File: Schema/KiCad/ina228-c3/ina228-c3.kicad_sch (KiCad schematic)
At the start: 35 parts, among them J1 Terminal, U1 XL7015E1, U2 HT7833, U3 INA238, U4 ESP32-C3-WROOM-02

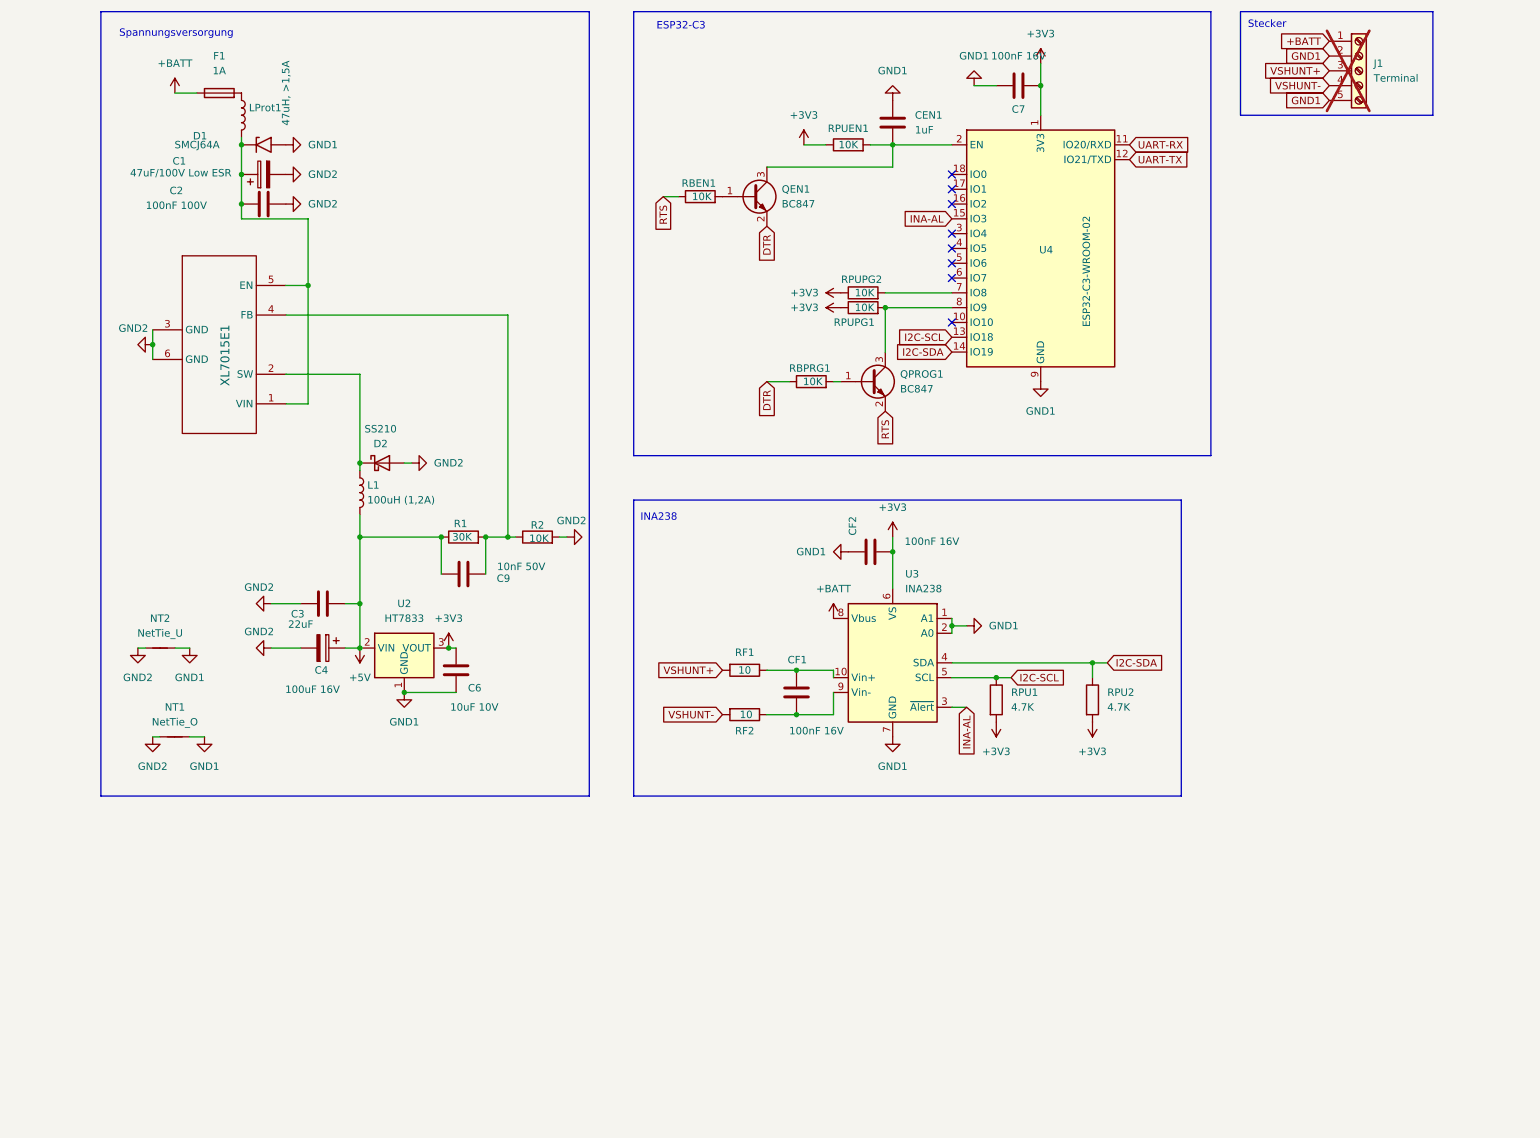
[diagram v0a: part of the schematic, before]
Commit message: Remove usb2uart chip, making the design simpler (but probably more expensive.)
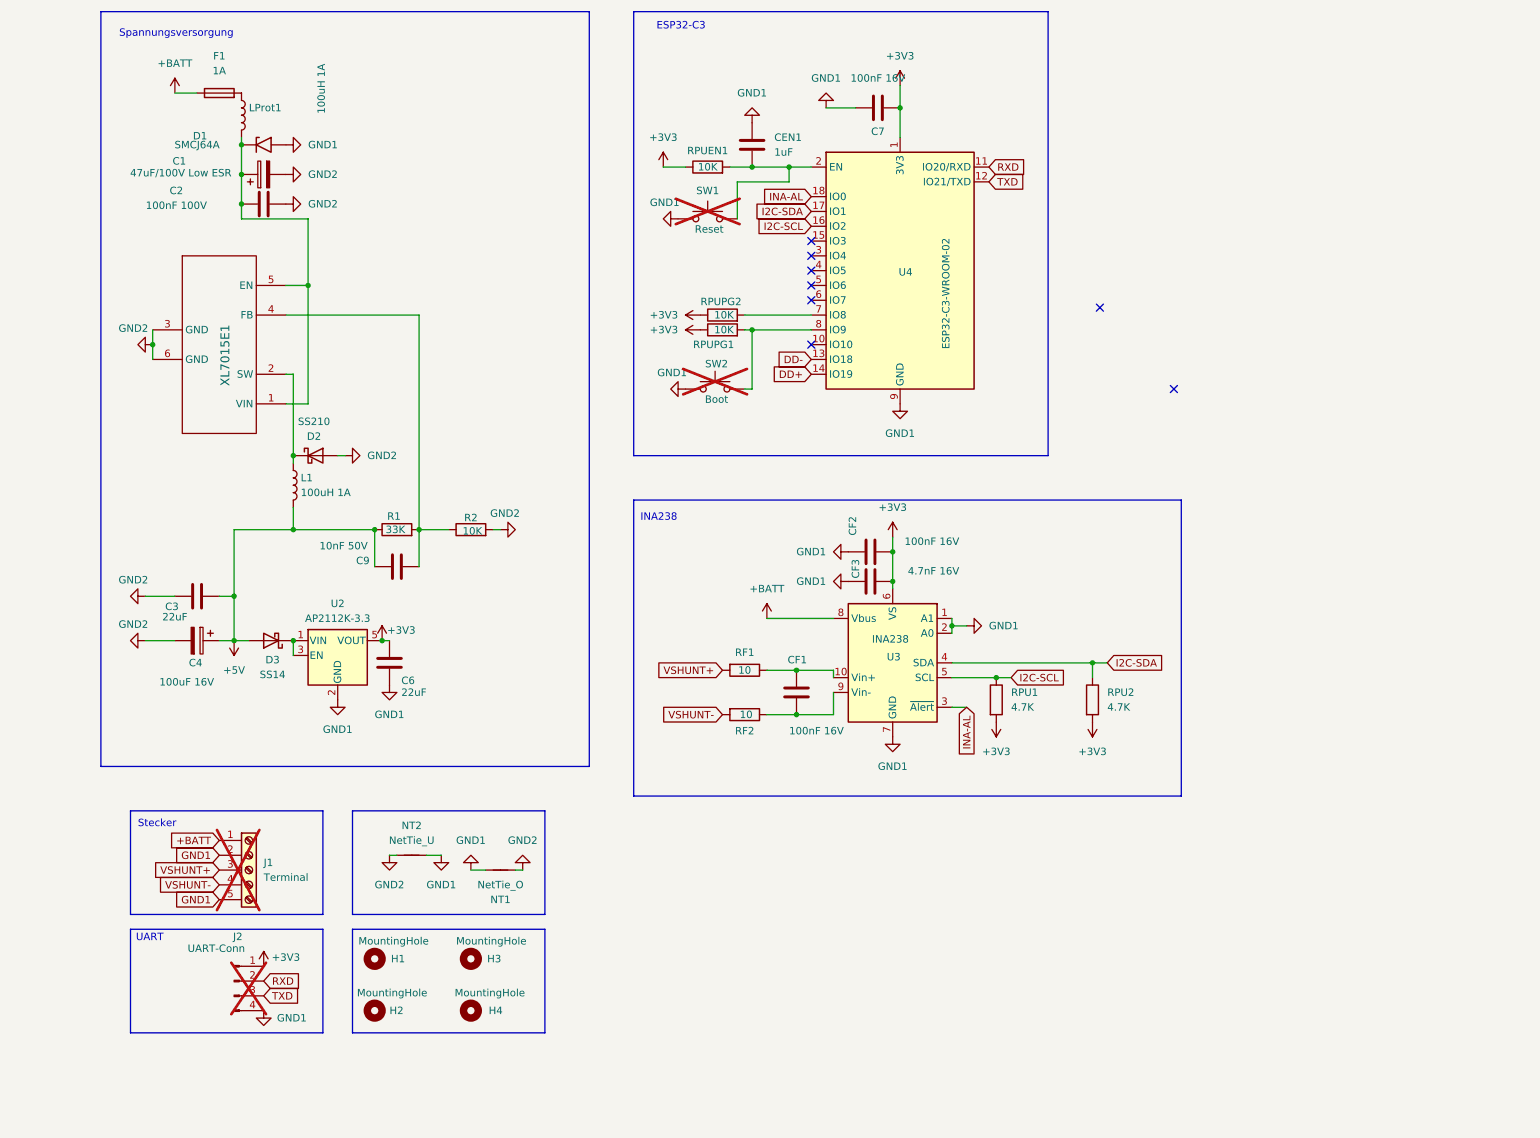
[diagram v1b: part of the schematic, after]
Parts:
- removed QEN1, QPROG1: BC847, Package_TO_SOT_SMD:SOT-23, symbol Transistor_BJT:BC847
- removed RBEN1, RBPRG1: 10K, Resistor_SMD:R_0603_1608Metric, symbol Device:R
- added CF3: 4.7nF 16V, Capacitor_SMD:C_0603_1608Metric, symbol Device:C
- added D3: SS14, Diode_SMD:D_SMA, symbol Diode:SS14
- added H1, H2, H3, H4: MountingHole, MountingHole:MountingHole_2.2mm_M2_DIN965, symbol Mechanical:MountingHole
- added J2: UART-Conn, Connector_PinHeader_2.54mm:PinHeader_1x04_P2.54mm_Vertical, symbol Connector:Conn_01x04_Pin
- added SW1: Reset, Button_Switch_THT:SW_PUSH_1P1T_6x3.5mm_H4.3_APEM_MJTP1243, symbol Switch:SW_Push
- added SW2: Boot, Button_Switch_THT:SW_PUSH_1P1T_6x3.5mm_H4.3_APEM_MJTP1243, symbol Switch:SW_Push
- C6: value 10uF 10V -> 22uF; LCSC C15850 -> C45783
- L1: value 100uH (1,2A) -> 100uH 1A; footprint Inductor_SMD:L_12x12mm_H6mm -> Inductor_SMD:L_TDK_VLS6045EX_VLS6045AF
- LProt1: value 47uH, >1,5A -> 100uH 1A; footprint Inductor_SMD:L_Sunlord_SWPA8040S -> Inductor_SMD:L_TDK_VLS6045EX_VLS6045AF
- R1: value 30K -> 33K; LCSC C22984 -> C4216
- U2: value HT7833 -> AP2112K-3.3; footprint Package_TO_SOT_SMD:SOT-89-3 -> Package_TO_SOT_SMD:SOT-23-5; symbol Regulator_Linear:HT75xx-1-SOT89 -> Regulator_Linear:AP2112K-3.3; LCSC C347195 -> C23380830
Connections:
- net +3V3: now also U2.5 (VOUT), CF3.2, J2.1 (Pin_1); no longer U2.3 (VOUT)
- net +5V: now also D3.2 (A); no longer U2.2 (VIN)
- net GND1: now also U2.2 (GND), CF3.1, J2.4 (Pin_4), SW1.1, SW2.1; no longer U2.1 (GND)
- net I2C-SCL: now also U4.16 (IO2); no longer U4.13 (IO18)
- net I2C-SDA: now also U4.17 (IO1); no longer U4.14 (IO19)
- net INA-AL: now also U4.18 (IO0); no longer U4.15 (IO3)
- net at CEN1.2, RPUEN1.2, U4.2 (EN): now also SW1.2
- net at RPUPG1.2, U4.8 (IO9): now also SW2.2
- net UART-RX renamed RXD
- net RXD: now also J2.2 (Pin_2)
- net UART-TX renamed TXD
- net TXD: now also J2.3 (Pin_3)
- new net: D3.1 (K), U2.1 (VIN), U2.3 (EN)
- new net DD+: U4.14 (IO19)
- new net DD-: U4.13 (IO18)
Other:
- note added: "UART"
- moved on the sheet: C3, C4, C6, C7, C9, CEN1, D2, J1, L1, NT1, NT2, R1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
